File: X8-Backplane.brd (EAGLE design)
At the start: 122.1 x 106.6 mm, 18 parts, among them U1 BD6221FSOP, U2 MIC29501-5.0WU, U3 MIC29501-5.0WU, U4 FQB27P06, U5 FQB27P06, U6 FQB27P06

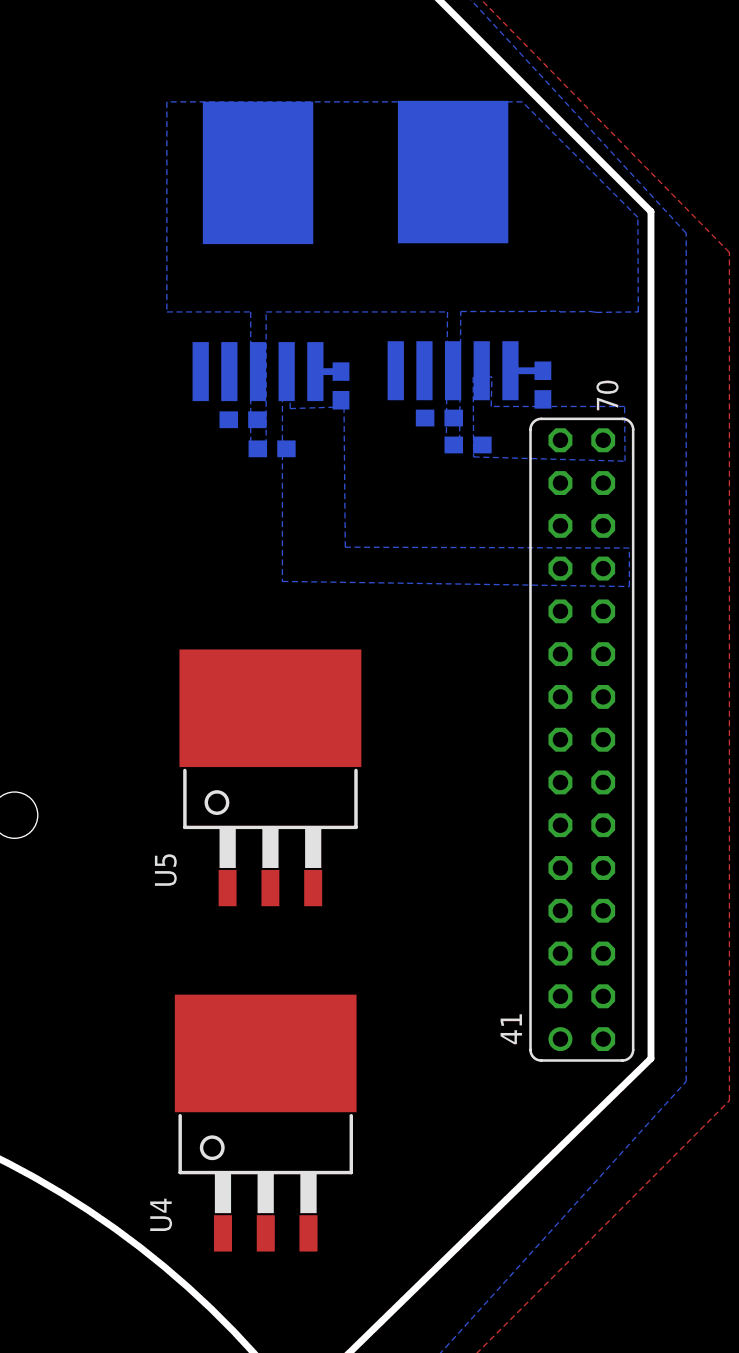
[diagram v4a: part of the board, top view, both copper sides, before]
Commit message: Started initial routing on the board
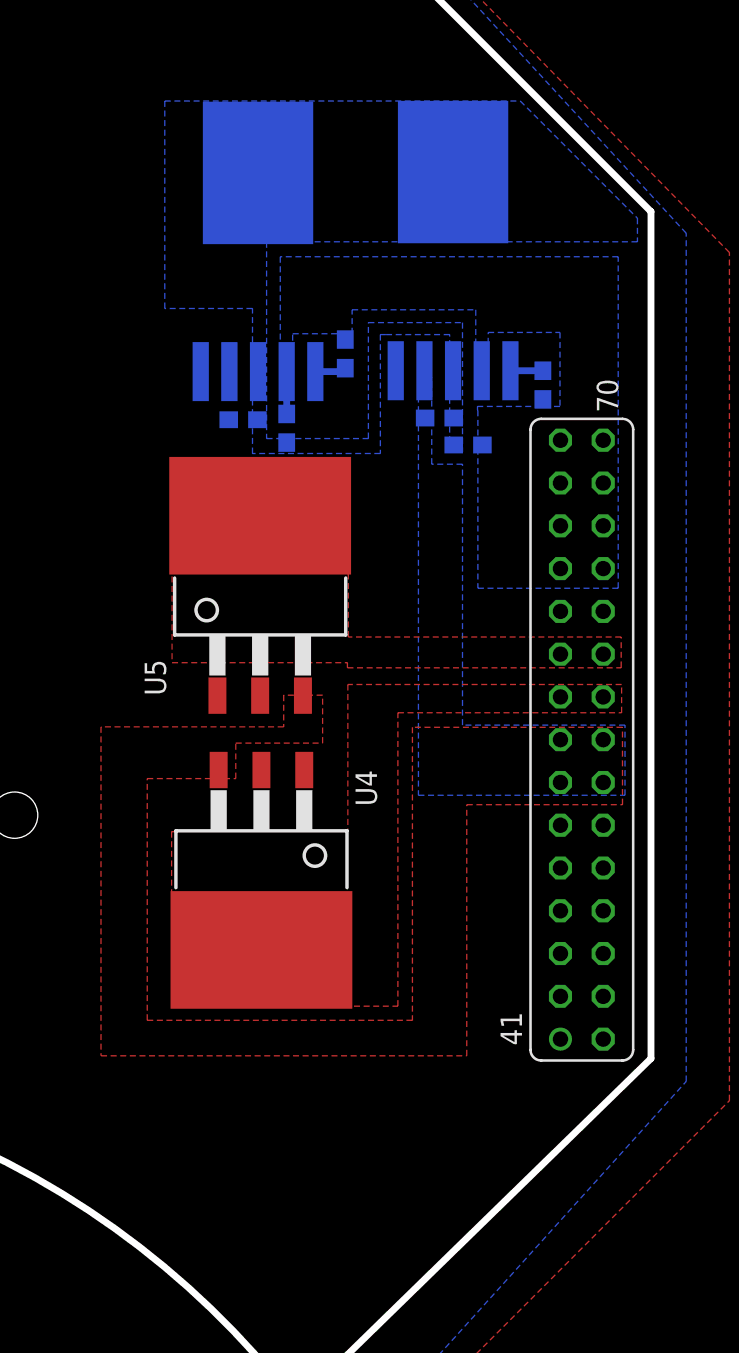
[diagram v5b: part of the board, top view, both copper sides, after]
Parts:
- moved U4 17.4 mm to (101.4, 25.1), turned to 180 degrees
- moved U5 11.4 mm to (101.3, 39.7)
- moved R1 1.92 mm to (106.3, 54.9), turned to 90 degrees
- moved C5 1.49 mm to (102.9, 50.5), turned to 270 degrees
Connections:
- removed net LASER_5V: U$4.57, U$4.58, U5.TAB
- removed net LED_5V: U$4.59, U$4.60, U4.TAB
- new net +5V_LASER: U$4.59, U$4.60, U5.TAB
- new net +5V_LED: U$4.57, U$4.58, U4.TAB
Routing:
- net +12V: track 0.00 -> 2.52 mm
- added copper zone on layer 1, net +5V_CAMERA_TUBE
- added copper zone on layer 16, net +5V_CAMERA_TUBE
- added copper zone on layer 1, net +5V_LASER
- added copper zone on layer 1, net +5V_LED

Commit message: Leaving the rest to Ryan, not sure I can work with the layout given to me
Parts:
- moved U6 15.1 mm to (23.8, 26.4)
- moved U1 5.60 mm to (10.9, 23.4)
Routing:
- net LED_ON: track 0.00 -> 71.8 mm, vias 0 -> 1
- net LASER_ON: track 0.00 -> 64.1 mm, vias 0 -> 1
- net 3.3V: track 0.00 -> 51.0 mm, vias 0 -> 1
- net FIN: track 0.00 -> 33.4 mm
- net BT_LED_ON: track 0.00 -> 25.3 mm
- net GND_PIEZO: track 0.00 -> 10.1 mm
- net +5V: track 0.00 -> 9.93 mm
- net 3V3_PIEZO: track 0.00 -> 7.35 mm
- net +12V: track 2.52 -> 9.29 mm
- net Y: track 0.00 -> 6.18 mm
- net Z: track 0.00 -> 5.65 mm
- net B: track 0.00 -> 5.13 mm
- net A: track 0.00 -> 4.90 mm
- added copper zone on layer 16, net +5V
- added copper zone on layer 1, net N$2

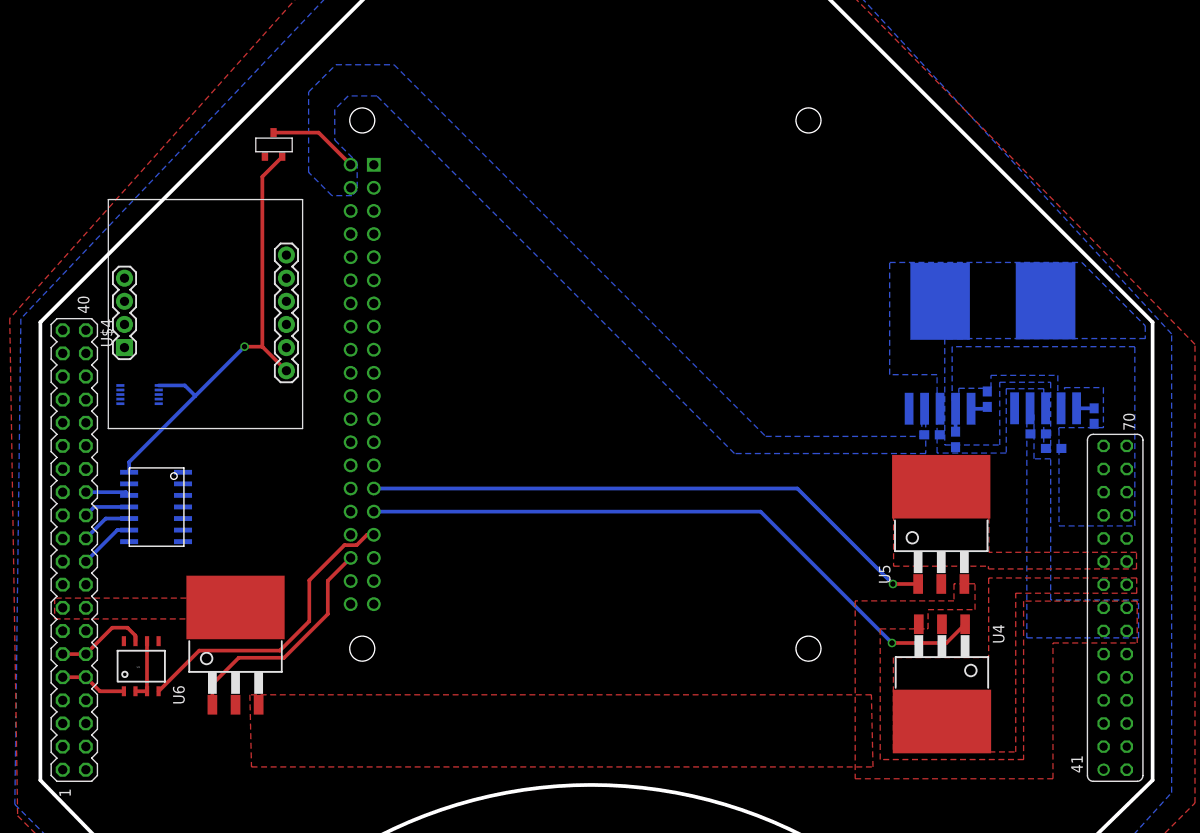
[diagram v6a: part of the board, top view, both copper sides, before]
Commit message: Redid routing and moved components
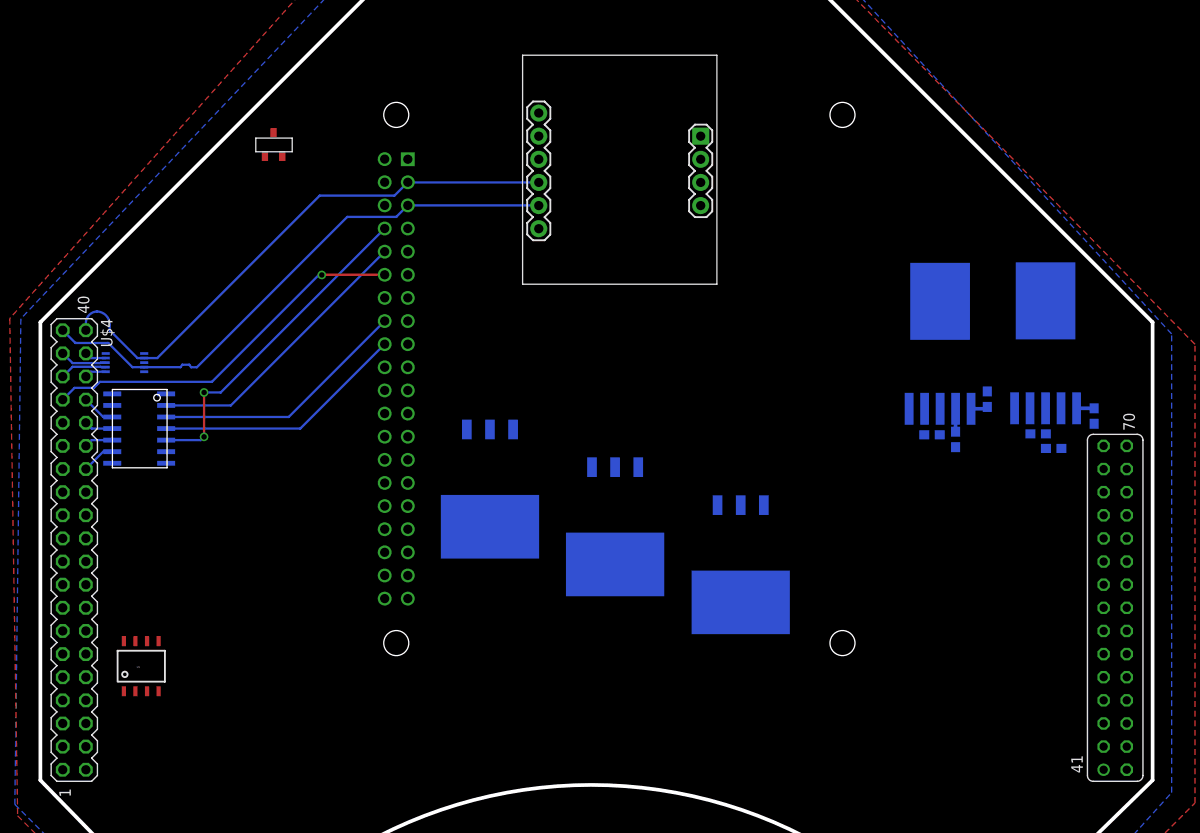
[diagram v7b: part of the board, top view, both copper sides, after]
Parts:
- moved U$3 49.0 mm to (66.0, 81.3), turned to 0 degrees
- moved U4 39.8 mm to (65.5, 42.4), flipped to the bottom
- moved U6 34.4 mm to (51.7, 46.5), flipped to the bottom, turned to 180 degrees
- moved U5 22.1 mm to (79.3, 38.2), flipped to the bottom, turned to 180 degrees
- moved U$1 8.81 mm to (16.2, 47.9)
- moved U$7 3.85 mm to (11.7, 58.9)
- moved PCB1 3.78 mm to (93.9, 89.6)
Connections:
- net A: now also U$4.34; no longer U$4.26
- net B: now also U$4.32; no longer U$4.24
- net SERVO_PWM: now also U$4.33; no longer U$4.30
- net Y: now also U$4.28; no longer U$4.20
- net Z: now also U$4.30; no longer U$4.22
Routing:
- net LED_ON: track 71.8 -> 0.00 mm, vias 1 -> 0
- net LASER_ON: track 64.1 -> 0.00 mm, vias 1 -> 0
- net SCL: track 0.00 -> 61.6 mm
- net SDA: track 0.00 -> 61.5 mm
- net 3.3V: track 51.0 -> 0.00 mm, vias 1 -> 0
- net SERVO_PWM: track 0.00 -> 41.0 mm, vias 0 -> 1
- net TX: track 0.00 -> 36.5 mm, vias 0 -> 2
- net FIN: track 33.4 -> 0.00 mm
- net RX: track 0.00 -> 31.0 mm
- net !RE: track 0.00 -> 28.4 mm
- net DE: track 0.00 -> 27.8 mm
- net BT_LED_ON: track 25.3 -> 0.00 mm
- net GND_PIEZO: track 10.1 -> 0.00 mm
- net +5V: track 9.93 -> 0.00 mm
- net 3V3_PIEZO: track 7.35 -> 0.00 mm
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- removed copper zone on layer 16, net +12V
- removed copper zone on layer 16, net +5V
- removed copper zone on layer 1, net +5V_CAMERA_TUBE
- removed copper zone on layer 16, net +5V_CAMERA_TUBE
- removed copper zone on layer 1, net +5V_LASER
- removed copper zone on layer 1, net +5V_LED
- removed copper zone on layer 1, net N$2

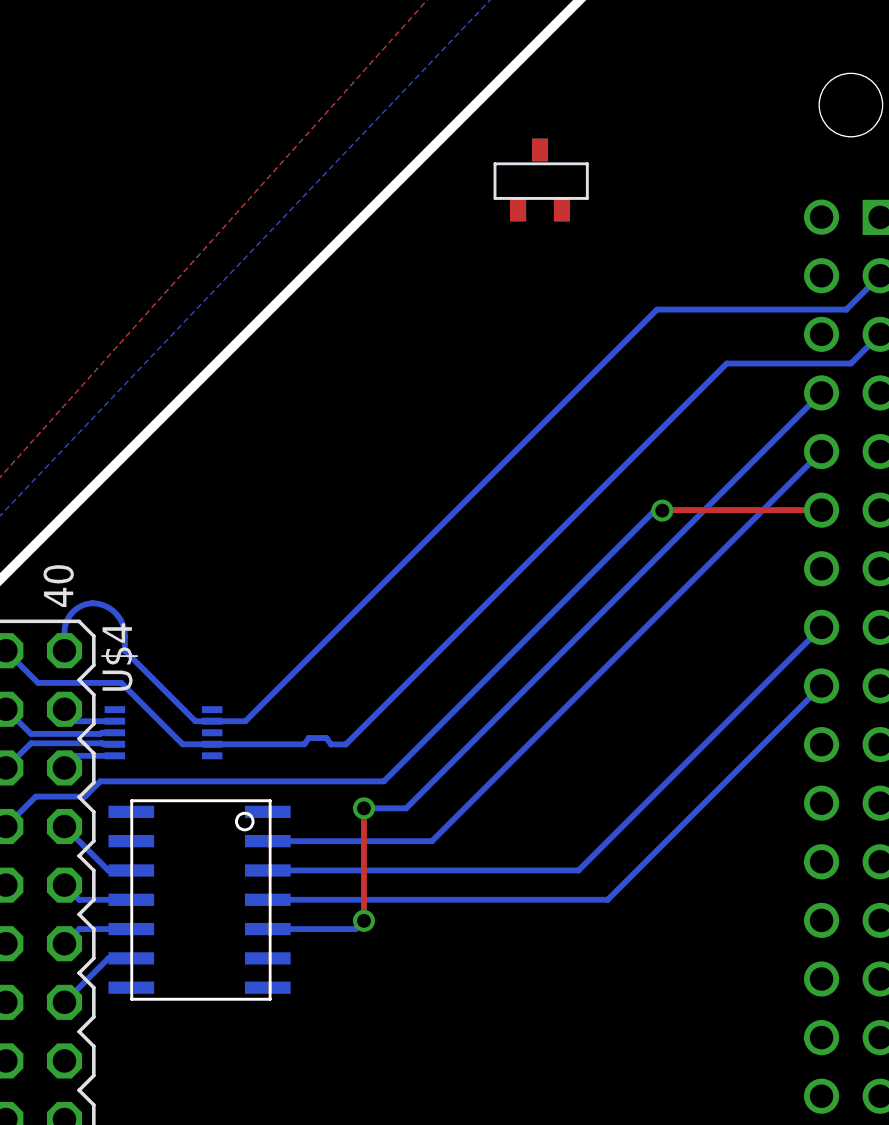
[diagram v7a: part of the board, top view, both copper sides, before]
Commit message: Moved some more components and added vias to reconnect isolated grounds
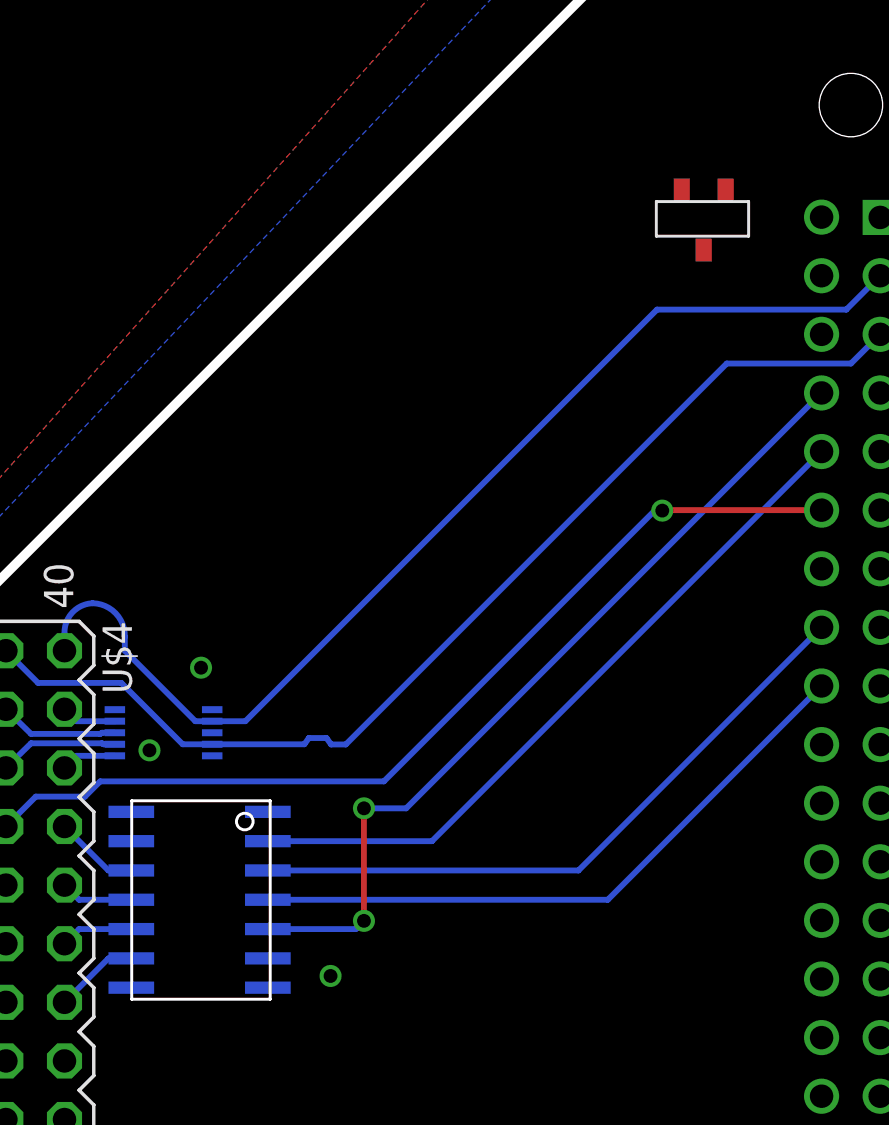
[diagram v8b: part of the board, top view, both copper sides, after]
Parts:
- moved U$5 9.03 mm to (36.0, 82.4), turned to 180 degrees
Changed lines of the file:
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@@
 <element name="U$1" library="BackplaneParts" package="MAX3491" value="MAX3491" x="16.1798" y="47.879" rot="MR0"/>
 <element name="U1" library="CamSensComponents" package="SOP8" value="BD6221FSOP" x="10.9474" y="23.3934"/>
-<element name="U$5" library="PowerComponents" package="SOT-23-3" value="AP2210" x="27.0256" y="81.5848"/>
+<element name="U$5" library="PowerComponents" package="SOT-23-3" value="AP2210" x="36.0172" y="82.4484" rot="R180"/>
 <element name="U4" library="CamSensComponents" package="TO263-3" value="FQB27P06" x="65.4812" y="42.3672" rot="MR180"/>
 <element name="U5" library="CamSensComponents" package="TO263-3" value="FQB27P06" x="79.2734" y="38.2016" rot="MR180"/>
@@
 <vertex x="38.5318" y="100.7364"/>
 </polygon>
-<wire x1="13.7681" y1="57.928" x2="16.1798" y2="49.149" width="0" layer="19" extent="16-16"/>
+<via x="18.8976" y="48.387" extent="1-16" drill="0.6"/>
+<via x="13.2842" y="61.7474" extent="1-16" drill="0.6"/>
+<via x="11.049" y="58.166" extent="1-16" drill="0.6"/>
 </signal>
 <signal name="+12V">
@@
 <wire x1="40.178" y1="78.735" x2="99.4664" y2="53.8607" width="0" layer="19" extent="16-16"/>
 <wire x1="40.178" y1="81.275" x2="40.178" y2="78.735" width="0" layer="19" extent="1-1"/>
-<wire x1="27.9756" y1="84.1848" x2="40.178" y2="81.275" width="0" layer="19" extent="1-1"/>
+<wire x1="35.0672" y1="79.8484" x2="40.178" y2="81.275" width="0" layer="19" extent="1-1"/>
 </signal>
 <signal name="EN1">
@@
 <contactref element="U6" pad="3"/>
 <wire x1="111.0878" y1="51.1048" x2="111.0488" y2="53.9115" width="0" layer="19" extent="16-16"/>
-<wire x1="81.8134" y1="43.2816" x2="111.0878" y2="51.1048" width="0" layer="19" extent="1-16"/>
-<wire x1="54.2798" y1="51.5874" x2="81.8134" y2="43.2816" width="0" layer="19" extent="1-1"/>
-<wire x1="119.126" y1="29.464" x2="54.2798" y2="51.5874" width="0" layer="19" extent="1-1"/>
-<wire x1="119.126" y1="32.004" x2="119.126" y2="29.464" width="0" layer="19" extent="1-1"/>
+<wire x1="119.126" y1="32.004" x2="111.0878" y2="51.1048" width="0" layer="19" extent="16-16"/>
 <wire x1="121.666" y1="32.004" x2="119.126" y2="32.004" width="0" layer="19" extent="1-1"/>
-<wire x1="121.666" y1="29.464" x2="119.126" y2="29.464" width="0" layer="19" extent="1-1"/>
-<wire x1="68.0212" y1="47.4472" x2="81.8134" y2="43.2816" width="0" layer="19" extent="1-1"/>
+<wire x1="121.666" y1="29.464" x2="121.666" y2="32.004" width="0" layer="19" extent="1-1"/>
+<wire x1="119.126" y1="29.464" x2="119.126" y2="32.004" width="0" layer="19" extent="1-1"/>
+<wire x1="81.8134" y1="43.2816" x2="111.0878" y2="51.1048" width="0" layer="19" extent="16-16"/>
+<wire x1="68.0212" y1="47.4472" x2="81.8134" y2="43.2816" width="0" layer="19" extent="16-16"/>
+<wire x1="54.2798" y1="51.5874" x2="68.0212" y2="47.4472" width="0" layer="19" extent="16-16"/>
 </signal>
 <signal name="3.3V">
@@
 <contactref element="U$1" pad="VCC14"/>
 <contactref element="U$1" pad="VCC13"/>
-<wire x1="28.9256" y1="81.5848" x2="57.0992" y2="86.3346" width="0" layer="19" extent="1-1"/>
-<wire x1="13.7681" y1="59.928" x2="28.9256" y2="81.5848" width="0" layer="19" extent="1-16"/>
+<wire x1="34.1172" y1="82.4484" x2="57.0992" y2="86.3346" width="0" layer="19" extent="1-1"/>
+<wire x1="13.7681" y1="59.928" x2="34.1172" y2="82.4484" width="0" layer="19" extent="1-16"/>
 <wire x1="9.5491" y1="59.928" x2="13.7681" y2="59.928" width="0" layer="19" extent="16-16"/>
 <wire x1="10.2613" y1="55.499" x2="9.5491" y2="59.928" width="0" layer="19" extent="16-16"/>
@@
 <contactref element="U$4" pad="57"/>
 <wire x1="119.126" y1="34.544" x2="121.666" y2="34.544" width="0" layer="19" extent="1-1"/>
-<wire x1="65.4812" y1="36.7665" x2="119.126" y2="34.544" width="0" layer="19" extent="1-1"/>
+<wire x1="65.4812" y1="36.7665" x2="119.126" y2="34.544" width="0" layer="19" extent="16-16"/>
 </signal>
 <signal name="+5V_LASER">
@@
 <contactref element="U$4" pad="59"/>
 <wire x1="119.126" y1="37.084" x2="121.666" y2="37.084" width="0" layer="19" extent="1-1"/>
-<wire x1="79.2734" y1="32.6009" x2="119.126" y2="37.084" width="0" layer="19" extent="1-1"/>
+<wire x1="79.2734" y1="32.6009" x2="119.126" y2="37.084" width="0" layer="19" extent="16-16"/>
 </signal>
 <signal name="LED_ON">
 <contactref element="U4" pad="1"/>
 <contactref element="PCB1" pad="P$31"/>
-<wire x1="42.718" y1="43.175" x2="62.9412" y2="47.4472" width="0" layer="19" extent="1-1"/>
+<wire x1="42.718" y1="43.175" x2="62.9412" y2="47.4472" width="0" layer="19" extent="16-16"/>
 </signal>
 <signal name="LASER_ON">
 <contactref element="U5" pad="1"/>
 <contactref element="PCB1" pad="P$29"/>
-<wire x1="42.718" y1="45.715" x2="76.7334" y2="43.2816" width="0" layer="19" extent="1-1"/>
+<wire x1="42.718" y1="45.715" x2="76.7334" y2="43.2816" width="0" layer="19" extent="16-16"/>
 </signal>
 <signal name="DSDAM">
@@
 <contactref element="U6" pad="1"/>
 <contactref element="PCB1" pad="P$36"/>
-<wire x1="40.178" y1="38.095" x2="49.1998" y2="51.5874" width="0" layer="19" extent="1-1"/>
+<wire x1="40.178" y1="38.095" x2="49.1998" y2="51.5874" width="0" layer="19" extent="16-16"/>
 </signal>
 <signal name="BT_LED_5V">
@@
 <contactref element="U$4" pad="15"/>
 <contactref element="U$4" pad="16"/>
-<wire x1="7.366" y1="32.004" x2="51.7398" y2="40.9067" width="0" layer="19" extent="1-1"/>
+<wire x1="7.366" y1="32.004" x2="51.7398" y2="40.9067" width="0" layer="19" extent="16-16"/>
 <wire x1="4.826" y1="32.004" x2="7.366" y2="32.004" width="0" layer="19" extent="1-1"/>
 </signal>
